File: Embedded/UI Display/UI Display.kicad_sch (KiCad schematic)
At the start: 8 parts, among them J1 HUB75 Input, J2 Vertical, J3 JST [D], J4 JST [D], U1 Input A, U2 Input B

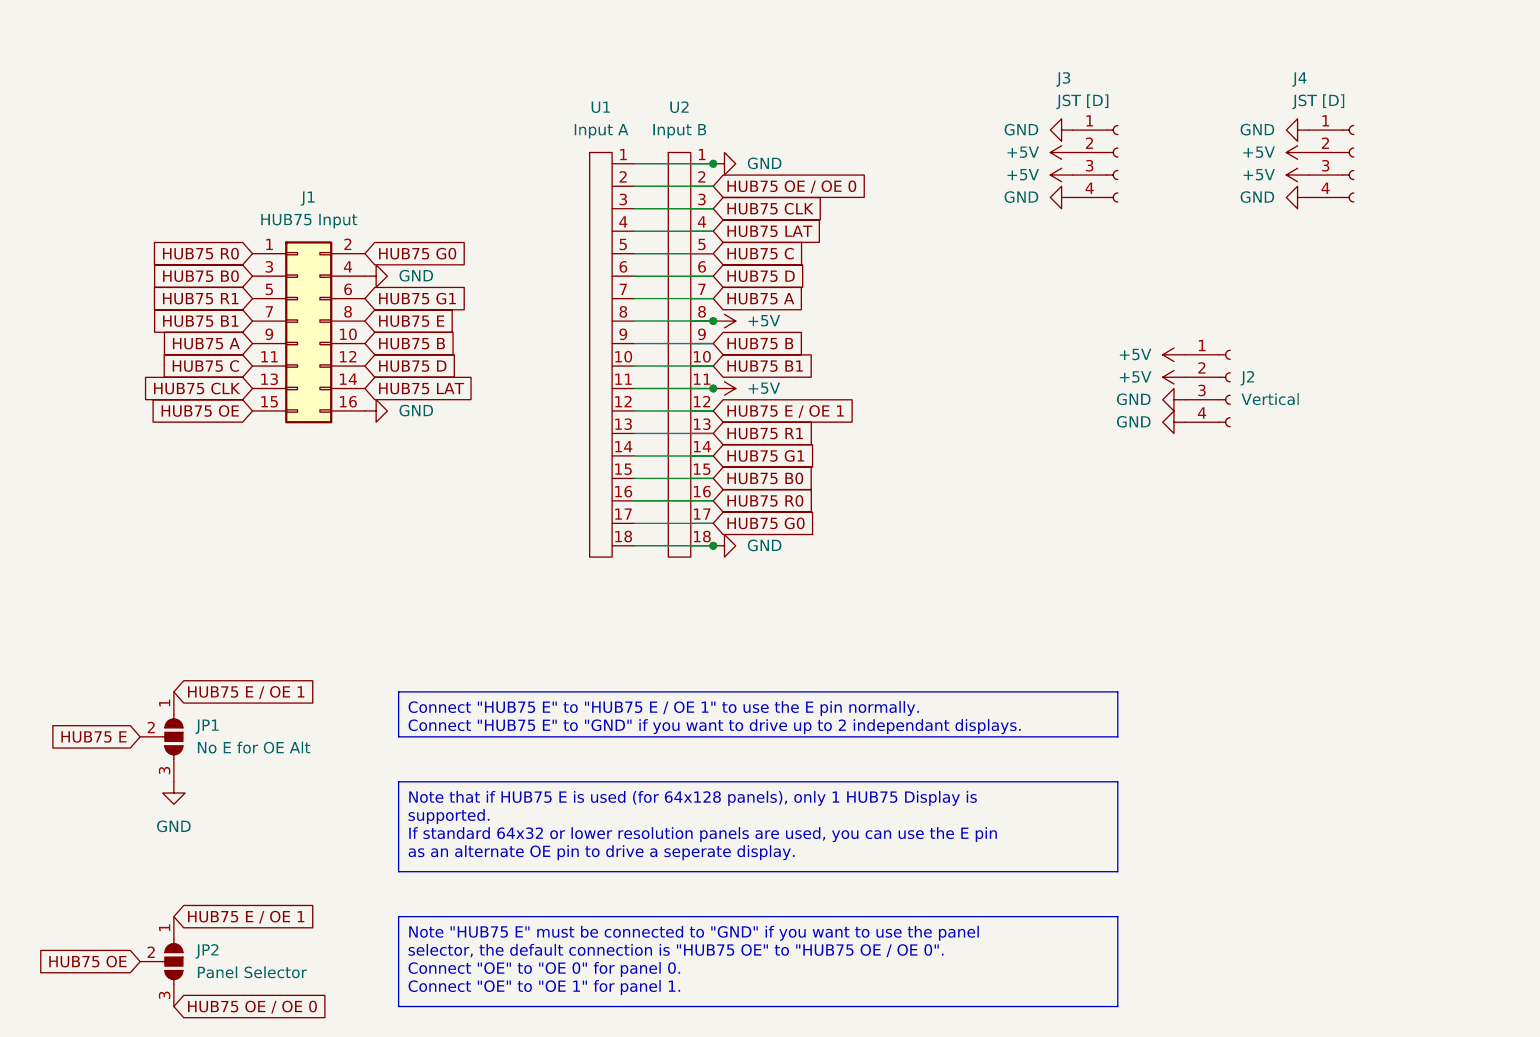
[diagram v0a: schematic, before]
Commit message: Added UI Display Schematic
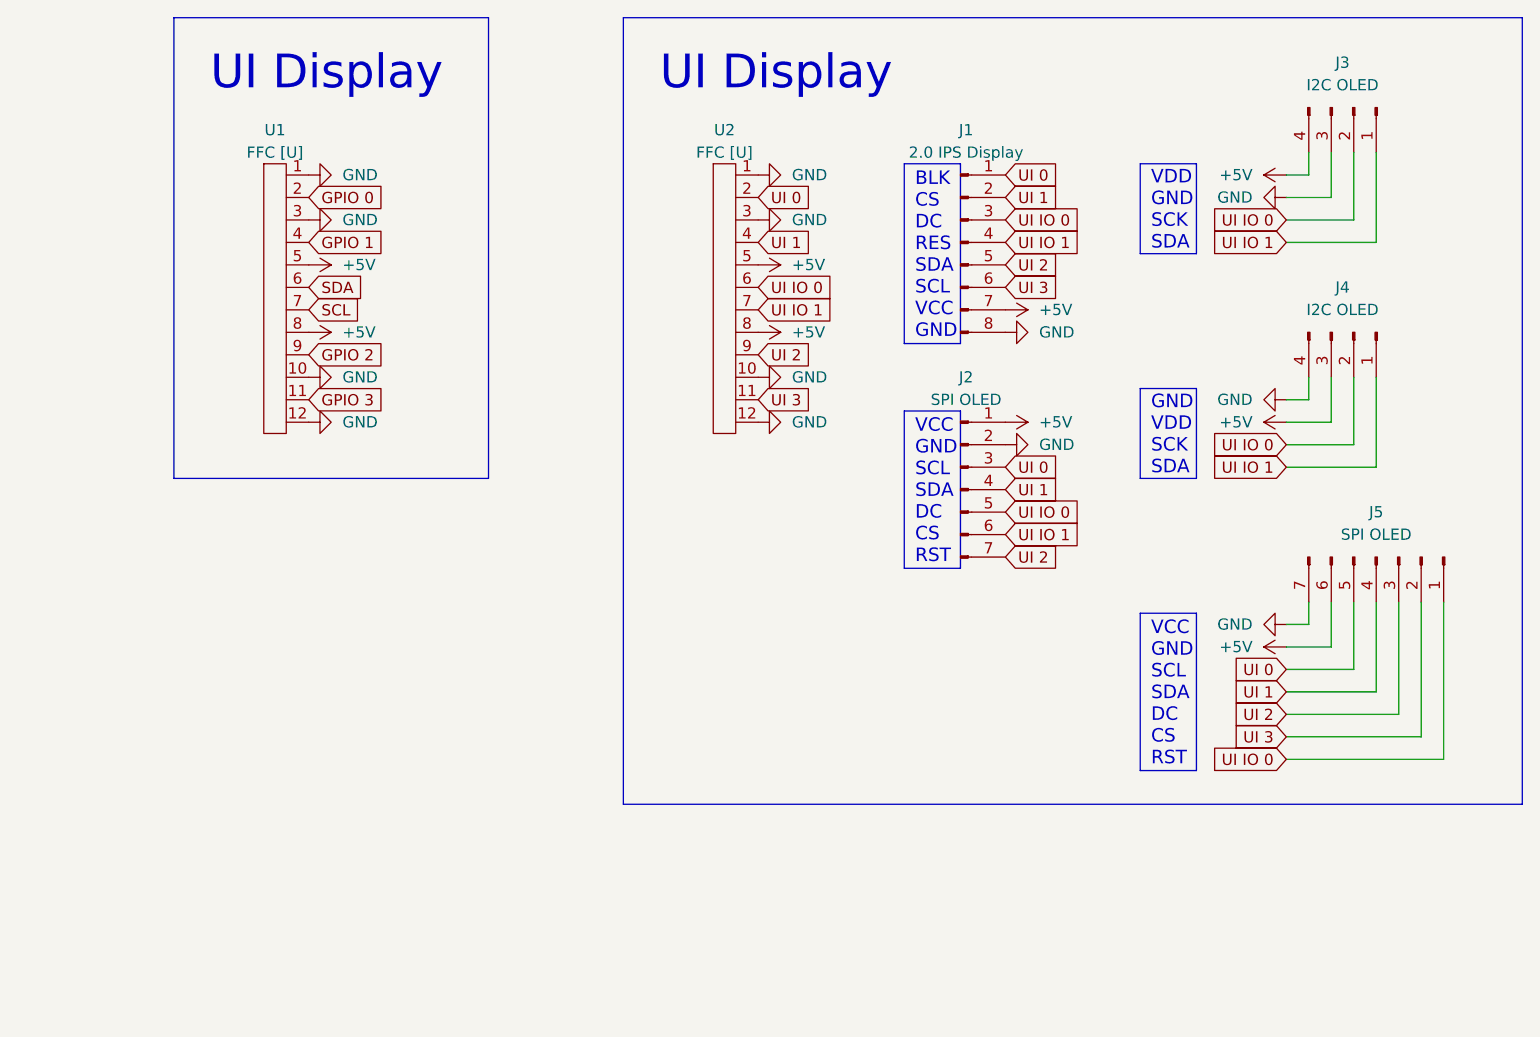
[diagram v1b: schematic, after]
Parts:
- removed J1: HUB75 Input, Connector_PinSocket_2.54mm:PinSocket_2x08_P2.54mm_Vertical, symbol Connector_Generic:Conn_02x08_Odd_Even
- removed J2: Vertical, Connector_Molex:Molex_KK-396_5273-04A_1x04_P3.96mm_Vertical, symbol Connector:Conn_01x04_Socket
- removed J3, J4: JST [D], Connector_Molex:Molex_PicoBlade_53048-0410_1x04_P1.25mm_Horizontal, symbol Connector:Conn_01x04_Socket
- removed JP1: No E for OE Alt, Jumper:SolderJumper-3_P1.3mm_Open_RoundedPad1.0x1.5mm_NumberLabels, symbol Jumper:SolderJumper_3_Open
- removed JP2: Panel Selector, Jumper:SolderJumper-3_P1.3mm_Open_RoundedPad1.0x1.5mm_NumberLabels, symbol Jumper:SolderJumper_3_Open
- removed U1: Input A, FFC_Connector:FFC Aliexpress 0.5mm 18P, symbol FCC_Connector:FFC_18P
- removed U2: Input B, FFC_Connector:FFC Aliexpress 0.5mm 18P, symbol FCC_Connector:FFC_18P
- added J1: 2.0 IPS Display, Connector_PinHeader_2.54mm:PinHeader_1x08_P2.54mm_Vertical, symbol Connector:Conn_01x08_Pin
- added J2, J5: SPI OLED, Connector_PinHeader_2.54mm:PinHeader_1x07_P2.54mm_Vertical, symbol Connector:Conn_01x07_Pin
- added J3, J4: I2C OLED, Connector_PinHeader_2.54mm:PinHeader_1x04_P2.54mm_Vertical, symbol Connector:Conn_01x04_Pin
- added U1, U2: FFC [U], FFC_Connector:FFC Aliexpress 0.5mm 12P, symbol FCC_Connector:FFC_12P
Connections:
- net +5V: now also J1.7 (Pin_7), J2.1 (Pin_1), J3.4 (Pin_4), J4.3 (Pin_3), J5.6 (Pin_6), U1.5, U1.8, U2.5, U2.8
- net GND: now also J1.8 (Pin_8), J2.2 (Pin_2), J3.3 (Pin_3), J4.4 (Pin_4), J5.7 (Pin_7), U1.1, U1.10, U1.12, U1.3, U2.1, U2.10, U2.12, U2.3
- new net GPIO 0: U1.2
- new net GPIO 1: U1.4
- new net GPIO 2: U1.9
- new net GPIO 3: U1.11
- new net SCL: U1.7
- new net SDA: U1.6
- new net UI 0: J1.1 (Pin_1), J2.3 (Pin_3), J5.5 (Pin_5), U2.2
- new net UI 1: J1.2 (Pin_2), J2.4 (Pin_4), J5.4 (Pin_4), U2.4
- new net UI 2: J1.5 (Pin_5), J2.7 (Pin_7), J5.3 (Pin_3), U2.9
- new net UI 3: J1.6 (Pin_6), J5.2 (Pin_2), U2.11
- new net UI IO 0: J1.3 (Pin_3), J2.5 (Pin_5), J3.2 (Pin_2), J4.2 (Pin_2), J5.1 (Pin_1), U2.6
- new net UI IO 1: J1.4 (Pin_4), J2.6 (Pin_6), J3.1 (Pin_1), J4.1 (Pin_1), U2.7
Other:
- note added: "UI Display"

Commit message: Added Rudimentary Routing
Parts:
- removed U1: FFC [U], FFC_Connector:FFC Aliexpress 0.5mm 12P, symbol FCC_Connector:FFC_12P
